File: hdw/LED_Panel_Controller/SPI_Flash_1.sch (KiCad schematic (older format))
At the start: 14 parts

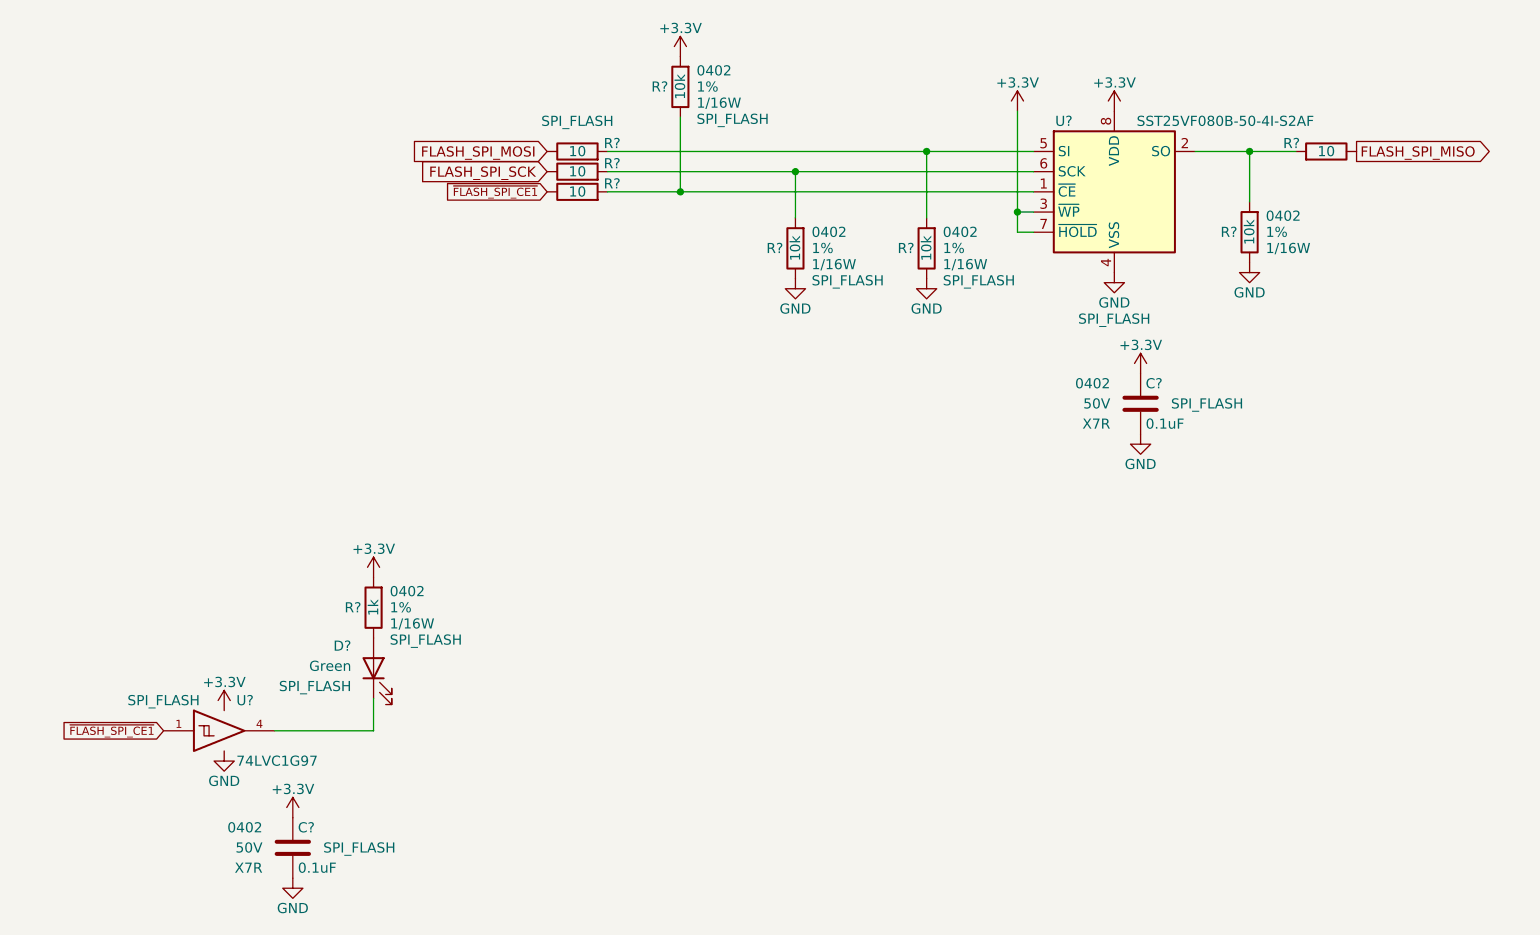
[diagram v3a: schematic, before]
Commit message: assigned I2C addresses
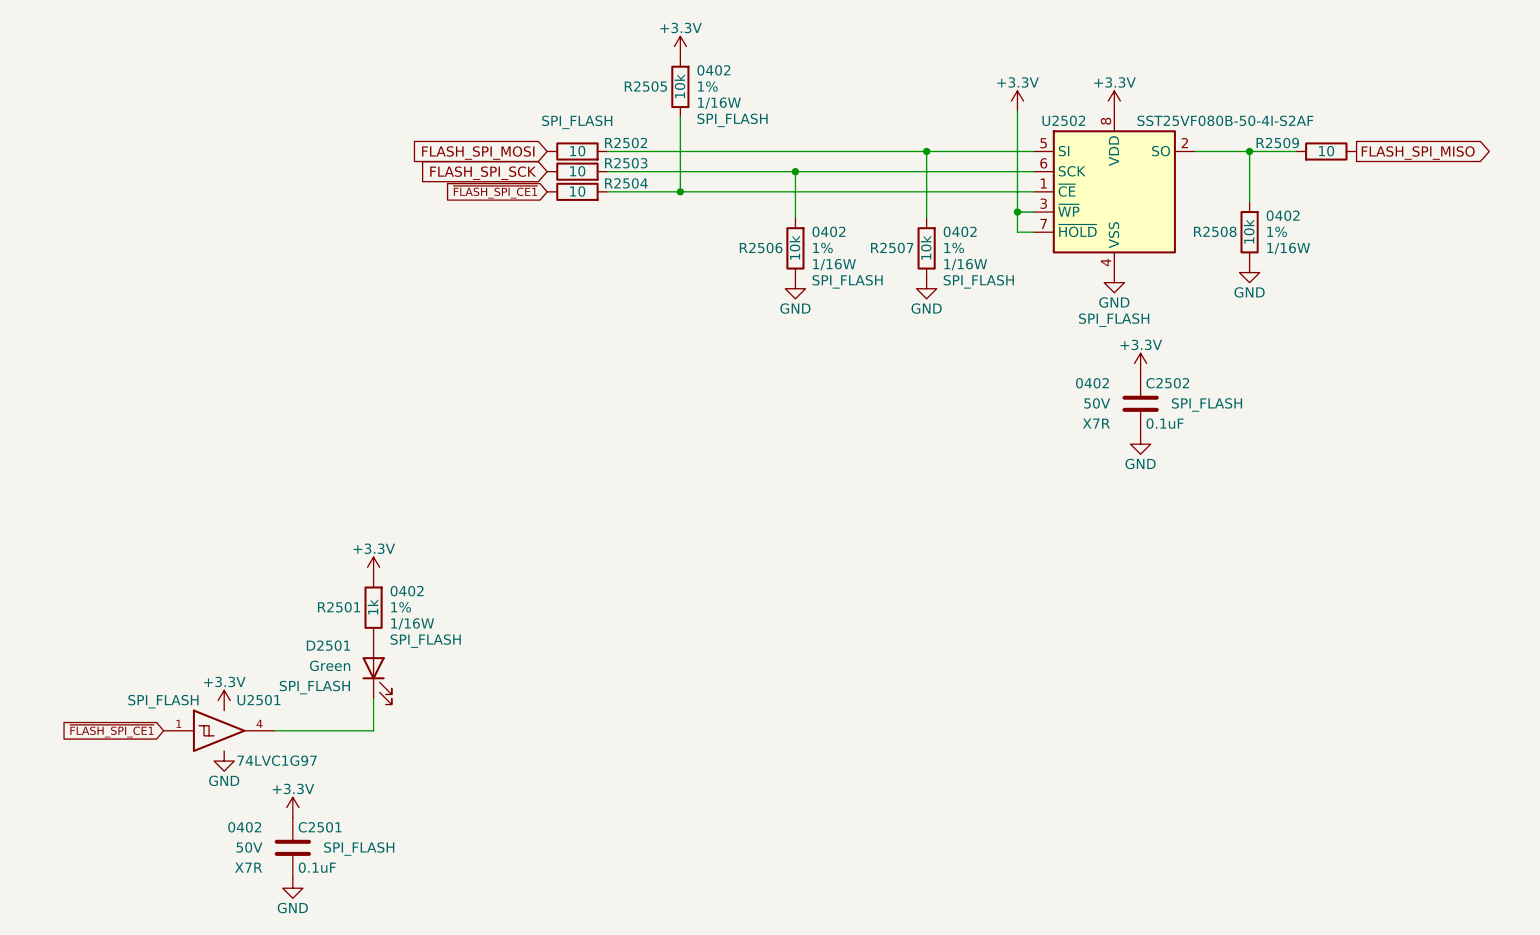
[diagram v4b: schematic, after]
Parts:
- removed C? (x2): 0.1uF, Capacitors_SMD:C_0402, symbol Custom_Library:C_Custom
- removed D?: Green, LEDs:LED_0402, symbol Device:LED
- removed R? (x4): 10, Resistors_SMD:R_0402, symbol Custom_Library:R_Custom
- removed R? (x3): 10k, Resistors_SMD:R_0402, symbol Custom_Library:R_Custom
- removed R?: 1k, Resistors_SMD:R_0402, symbol Custom_Library:R_Custom
- removed U?: 74LVC1G97, Package_TO_SOT_SMD:SOT-363_SC-70-6, symbol Custom_Library:74LVC1G97_Power_BUF
- added C2501, C2502: 0.1uF, Capacitors_SMD:C_0402, symbol Custom_Library:C_Custom
- added D2501: Green, LEDs:LED_0402, symbol Device:LED
- added R2501: 1k, Resistors_SMD:R_0402, symbol Custom_Library:R_Custom
- added R2502, R2503, R2504, R2509: 10, Resistors_SMD:R_0402, symbol Custom_Library:R_Custom
- added R2505, R2506, R2507: 10k, Resistors_SMD:R_0402, symbol Custom_Library:R_Custom
- added U2501: 74LVC1G97, Package_TO_SOT_SMD:SOT-363_SC-70-6, symbol Custom_Library:74LVC1G97_Power_BUF
- gave numbers to parts that had none: 2
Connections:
- net +3V3: now also C2501.1, C2502.1, R2501.1, R2505.1, U2501.5 (VCC)
- net FLASH_SPI_MISO: now also R2509.2
- net FLASH_SPI_MOSI: now also R2502.2
- net FLASH_SPI_SCK: now also R2503.2
- net GND: now also C2501.2, C2502.2, R2506.2, R2507.2, U2501.2 (GND), U2501.3 (GND), U2501.6 (GND)
- net ~FLASH_SPI_CE1: now also R2504.2, U2501.1
- net at R2508.1, U2502.2 (SO): now also R2509.1
- net at U2502.5 (SI): now also R2502.1, R2507.1
- net at U2502.1 (~CE): now also R2504.1, R2505.2
- net at U2502.6 (SCK): now also R2503.1, R2506.1
- new net: D2501.1 (K), U2501.4
- new net: D2501.2 (A), R2501.2
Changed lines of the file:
@@
 $EndDescr
 $Comp
-L power:GND #PWR?
+L power:GND #PWR02511
 U 1 1 5BB4E0E3
 P 6080 4050
-F 0 "#PWR?" H 6080 3800 50  0001 C CNN
+F 0 "#PWR02511" H 6080 3800 50  0001 C CNN
 F 1 "GND" H 6080 3900 50  0000 C CNN
 F 2 "" H 6080 4050 50  0001 C CNN
@@
 $EndComp
 $Comp
-L Custom_Library:R_Custom R?
+L Custom_Library:R_Custom R2508
 U 1 1 5BB4EDD1
 P 6750 3850
-F 0 "R?" H 6690 3850 50  0000 R CNN
+F 0 "R2508" H 6690 3850 50  0000 R CNN
 F 1 "10k" V 6750 3850 50  0000 C CNN
 F 2 "Resistors_SMD:R_0402" H 6750 3850 50  0001 C CNN
@@
 $EndComp
 $Comp
-L power:GND #PWR?
+L power:GND #PWR02508
 U 1 1 5BB4EE63
 P 5150 4080
-F 0 "#PWR?" H 5150 3830 50  0001 C CNN
+F 0 "#PWR02508" H 5150 3830 50  0001 C CNN
 F 1 "GND" H 5150 3930 50  0000 C CNN
 F 2 "" H 5150 4080 50  0001 C CNN
@@
 $EndComp
 $Comp
-L power:GND #PWR?
-U 1 1 5BB4EE7C
+L power:GND #PWR02514
+U 1 1 60786274
 P 6750 4000
-F 0 "#PWR?" H 6750 3750 50  0001 C CNN
+F 0 "#PWR02514" H 6750 3750 50  0001 C CNN
 F 1 "GND" H 6750 3850 50  0000 C CNN
 F 2 "" H 6750 4000 50  0001 C CNN
@@
 $EndComp
 $Comp
-L Custom_Library:R_Custom R?
-U 1 1 5BB4F53B
+L Custom_Library:R_Custom R2502
+U 1 1 6078627F
 P 3420 3450
-F 0 "R?" V 3380 3580 50  0000 L CNN
+F 0 "R2502" V 3380 3580 50  0000 L CNN
 F 1 "10" V 3420 3450 50  0000 C CNN
 F 2 "Resistors_SMD:R_0402" H 3420 3450 50  0001 C CNN
@@
 	3570 3650 3930 3650
 $Comp
-L power:+3.3V #PWR?
-U 1 1 5BDF3D33
+L power:+3.3V #PWR02506
+U 1 1 60786286
 P 3930 2980
-F 0 "#PWR?" H 3930 2830 50  0001 C CNN
+F 0 "#PWR02506" H 3930 2830 50  0001 C CNN
 F 1 "+3.3V" H 3930 3120 50  0000 C CNN
 F 2 "" H 3930 2980 50  0001 C CNN
@@
 $EndComp
 $Comp
-L power:+3.3V #PWR?
-U 1 1 5BDF3DF4
+L power:+3.3V #PWR02510
+U 1 1 6078628D
 P 6080 3250
-F 0 "#PWR?" H 6080 3100 50  0001 C CNN
+F 0 "#PWR02510" H 6080 3100 50  0001 C CNN
 F 1 "+3.3V" H 6080 3390 50  0000 C CNN
 F 2 "" H 6080 3250 50  0001 C CNN
@@
 $Comp
 L Custom_Library:C_Custom C?
-U 1 1 5C15F697
+U 1 1 60786292
 P 2010 6900
-AR Path="/5BAAE16C/5C15F697" Ref="C?"  Part="1"
-AR Path="/5BB181D8/5C15F697" Ref="C?"  Part="1"
-AR Path="/5BB2595E/5C15F697" Ref="C?"  Part="1"
-AR Path="/5F583577/5C15F697" Ref="C?"  Part="1"
-AR Path="/5F58358C/5C15F697" Ref="C?"  Part="1"
-F 0 "C?" H 2035 7000 50  0000 L CNN
+AR Path="/5BAAE16C/60786292" Ref="C?"  Part="1"
+AR Path="/5BB181D8/60786292" Ref="C?"  Part="1"
+AR Path="/5BB2595E/60786292" Ref="C?"  Part="1"
+AR Path="/5F583577/60786292" Ref="C?"  Part="1"
+AR Path="/5F58358C/60786292" Ref="C2501"  Part="1"
+F 0 "C2501" H 2035 7000 50  0000 L CNN
 F 1 "0.1uF" H 2035 6800 50  0000 L CNN
 F 2 "Capacitors_SMD:C_0402" H 2048 6750 50  0001 C CNN
@@
 $EndComp
 $Comp
-L power:+3.3V #PWR?
-U 1 1 5C161B83
+L power:+3.3V #PWR02501
+U 1 1 60786296
 P 1670 6220
-F 0 "#PWR?" H 1670 6070 50  0001 C CNN
+F 0 "#PWR02501" H 1670 6070 50  0001 C CNN
 F 1 "+3.3V" H 1670 6360 50  0000 C CNN
 F 2 "" H 1670 6220 50  0001 C CNN
@@
 $EndComp
 $Comp
-L power:+3.3V #PWR?
-U 1 1 5C161BE9
+L power:+3.3V #PWR02503
+U 1 1 607862A2
 P 2010 6750
-F 0 "#PWR?" H 2010 6600 50  0001 C CNN
+F 0 "#PWR02503" H 2010 6600 50  0001 C CNN
 F 1 "+3.3V" H 2010 6890 50  0000 C CNN
 F 2 "" H 2010 6750 50  0001 C CNN
@@
 $EndComp
 $Comp
-L power:GND #PWR?
-U 1 1 5C161C44
+L power:GND #PWR02504
+U 1 1 607862A6
 P 2010 7050
-F 0 "#PWR?" H 2010 6800 50  0001 C CNN
+F 0 "#PWR02504" H 2010 6800 50  0001 C CNN
 F 1 "GND" H 2010 6900 50  0000 C CNN
 F 2 "" H 2010 7050 50  0001 C CNN
@@
 $EndComp
 $Comp
-L power:GND #PWR?
+L power:GND #PWR02502
 U 1 1 5C161C9F
 P 1670 6420
-F 0 "#PWR?" H 1670 6170 50  0001 C CNN
+F 0 "#PWR02502" H 1670 6170 50  0001 C CNN
 F 1 "GND" H 1670 6270 50  0000 C CNN
 F 2 "" H 1670 6420 50  0001 C CNN
@@
 $Comp
 L power:+3.3V #PWR?
-U 1 1 5C166A81
+U 1 1 607862B4
 P 2410 5560
-AR Path="/5BB844FD/5C166A81" Ref="#PWR?"  Part="1"
-AR Path="/5BF346B3/5C166A81" Ref="#PWR?"  Part="1"
-AR Path="/5BB2595E/5C166A81" Ref="#PWR?"  Part="1"
-AR Path="/5F583577/5C166A81" Ref="#PWR?"  Part="1"
-AR Path="/5F58358C/5C166A81" Ref="#PWR?"  Part="1"
-F 0 "#PWR?" H 2410 5410 50  0001 C CNN
+AR Path="/5BB844FD/607862B4" Ref="#PWR?"  Part="1"
+AR Path="/5BF346B3/607862B4" Ref="#PWR?"  Part="1"
+AR Path="/5BB2595E/607862B4" Ref="#PWR?"  Part="1"
+AR Path="/5F583577/607862B4" Ref="#PWR?"  Part="1"
+AR Path="/5F58358C/607862B4" Ref="#PWR02505"  Part="1"
+F 0 "#PWR02505" H 2410 5410 50  0001 C CNN
 F 1 "+3.3V" H 2410 5700 50  0000 C CNN
 F 2 "" H 2410 5560 50  0001 C CNN
@@
 $Comp
 L Device:LED D?
-U 1 1 5C166A95
+U 1 1 607862B9
 P 2410 6010
-AR Path="/5BB844FD/5C166A95" Ref="D?"  Part="1"
-AR Path="/5BF346B3/5C166A95" Ref="D?"  Part="1"
-AR Path="/5BB2595E/5C166A95" Ref="D?"  Part="1"
-AR Path="/5F583577/5C166A95" Ref="D?"  Part="1"
-AR Path="/5F58358C/5C166A95" Ref="D?"  Part="1"
-F 0 "D?" V 2520 6120 50  0000 L CNN
+AR Path="/5BB844FD/607862B9" Ref="D?"  Part="1"
+AR Path="/5BF346B3/607862B9" Ref="D?"  Part="1"
+AR Path="/5BB2595E/607862B9" Ref="D?"  Part="1"
+AR Path="/5F583577/607862B9" Ref="D?"  Part="1"
+AR Path="/5F58358C/607862B9" Ref="D2501"  Part="1"
+F 0 "D2501" V 2520 6120 50  0000 L CNN
 F 1 "Green" V 2420 6120 50  0000 L CNN
 F 2 "LEDs:LED_0402" H 2410 6010 50  0001 C CNN
@@
 $EndComp
 $Comp
-L Memory_Flash:SST25VF080B-50-4x-S2Ax U?
+L Memory_Flash:SST25VF080B-50-4x-S2Ax U2502
 U 1 1 5F6879D5
 P 6080 3650
-F 0 "U?" H 5830 4000 50  0000 C CNN
+F 0 "U2502" H 5830 4000 50  0000 C CNN
 F 1 "SST25VF080B-50-4I-S2AF" H 6630 4000 50  0000 C CNN
 F 2 "Package_SO:SOIC-8_5.275x5.275mm_P1.27mm" H 6080 2950 50  0001 C CNN
@@
 $EndComp
 $Comp
-L power:+3.3V #PWR?
-U 1 1 5F689292
+L power:+3.3V #PWR02512
+U 1 1 60786300
 P 6210 4550
-F 0 "#PWR?" H 6210 4400 50  0001 C CNN
+F 0 "#PWR02512" H 6210 4400 50  0001 C CNN
 F 1 "+3.3V" H 6210 4690 50  0000 C CNN
 F 2 "" H 6210 4550 50  0001 C CNN
@@
 $EndComp
 $Comp
-L power:GND #PWR?
-U 1 1 5F689298
+L power:GND #PWR02513
+U 1 1 60786304
 P 6210 4850
-F 0 "#PWR?" H 6210 4600 50  0001 C CNN
+F 0 "#PWR02513" H 6210 4600 50  0001 C CNN
 F 1 "GND" H 6210 4700 50  0000 C CNN
 F 2 "" H 6210 4850 50  0001 C CNN
@@
 $EndComp
 $Comp
-L power:+3.3V #PWR?
-U 1 1 5F69329F
+L power:+3.3V #PWR02509
+U 1 1 6078630D
 P 5600 3250
-F 0 "#PWR?" H 5600 3100 50  0001 C CNN
+F 0 "#PWR02509" H 5600 3100 50  0001 C CNN
 F 1 "+3.3V" H 5600 3390 50  0000 C CNN
 F 2 "" H 5600 3250 50  0001 C CNN
@@
 	3570 3550 4500 3550
 $Comp
-L Custom_Library:R_Custom R?
-U 1 1 5F697048
+L Custom_Library:R_Custom R2506
+U 1 1 60786317
 P 4500 3930
-F 0 "R?" H 4440 3930 50  0000 R CNN
+F 0 "R2506" H 4440 3930 50  0000 R CNN
 F 1 "10k" V 4500 3930 50  0000 C CNN
 F 2 "Resistors_SMD:R_0402" H 4500 3930 50  0001 C CNN
@@
 $EndComp
 $Comp
-L power:GND #PWR?
-U 1 1 5F697052
+L power:GND #PWR02507
+U 1 1 6078631C
 P 4500 4080
-F 0 "#PWR?" H 4500 3830 50  0001 C CNN
+F 0 "#PWR02507" H 4500 3830 50  0001 C CNN
 F 1 "GND" H 4500 3930 50  0000 C CNN
 F 2 "" H 4500 4080 50  0001 C CNN
@@
 	4500 3550 5680 3550
 $Comp
-L Custom_Library:R_Custom R?
-U 1 1 5F7379BB
+L Custom_Library:R_Custom R2503
+U 1 1 60786326
 P 3420 3550
-F 0 "R?" V 3380 3680 50  0000 L CNN
+F 0 "R2503" V 3380 3680 50  0000 L CNN
 F 1 "10" V 3420 3550 50  0000 C CNN
 F 2 "Resistors_SMD:R_0402" H 3420 3550 50  0001 C CNN
@@
 $EndComp
 $Comp
-L Custom_Library:R_Custom R?
-U 1 1 5F737B74
+L Custom_Library:R_Custom R2504
+U 1 1 60786328
 P 3420 3650
-F 0 "R?" V 3380 3780 50  0000 L CNN
+F 0 "R2504" V 3380 3780 50  0000 L CNN
 F 1 "10" V 3420 3650 50  0000 C CNN
 F 2 "Resistors_SMD:R_0402" H 3420 3650 50  0001 C CNN
@@
 $EndComp
 $Comp
-L Custom_Library:R_Custom R?
-U 1 1 5F737D15
+L Custom_Library:R_Custom R2509
+U 1 1 60786330
 P 7130 3450
-F 0 "R?" V 7090 3580 50  0000 L CNN
+F 0 "R2509" V 7090 3580 50  0000 L CNN
 F 1 "10" V 7130 3450 50  0000 C CNN
 F 2 "Resistors_SMD:R_0402" H 7130 3450 50  0001 C CNN
@@
 $EndComp
 $Comp
-L Custom_Library:74LVC1G97_Power_BUF U?
-U 1 1 5FE9D8D5
+L Custom_Library:74LVC1G97_Power_BUF U2501
+U 1 1 60786346
 P 1670 6320
-F 0 "U?" H 1730 6470 50  0000 L CNN
+F 0 "U2501" H 1730 6470 50  0000 L CNN
 F 1 "74LVC1G97" H 1730 6170 50  0000 L CNN
 F 2 "Package_TO_SOT_SMD:SOT-363_SC-70-6" H 1720 6320 50  0001 C CNN
@@
 $EndComp
 $Comp
-L Custom_Library:R_Custom R?
-U 1 1 6026393A
+L Custom_Library:R_Custom R2507
+U 1 1 6078635A
 P 5150 3930
-F 0 "R?" H 5090 3930 50  0000 R CNN
+F 0 "R2507" H 5090 3930 50  0000 R CNN
 F 1 "10k" V 5150 3930 50  0000 C CNN
 F 2 "Resistors_SMD:R_0402" H 5150 3930 50  0001 C CNN
@@
 $EndComp
 $Comp
-L Custom_Library:R_Custom R?
-U 1 1 60263FB7
+L Custom_Library:R_Custom R2505
+U 1 1 6078635D
 P 3930 3130
-F 0 "R?" H 3870 3130 50  0000 R CNN
+F 0 "R2505" H 3870 3130 50  0000 R CNN
 F 1 "10k" V 3930 3130 50  0000 C CNN
 F 2 "Resistors_SMD:R_0402" H 3930 3130 50  0001 C CNN
@@
 $EndComp
 $Comp
-L Custom_Library:R_Custom R?
-U 1 1 60266213
+L Custom_Library:R_Custom R2501
+U 1 1 60786363
 P 2410 5710
-F 0 "R?" H 2350 5710 50  0000 R CNN
+F 0 "R2501" H 2350 5710 50  0000 R CNN
 F 1 "1k" V 2410 5710 50  0000 C CNN
 F 2 "Resistors_SMD:R_0402" H 2410 5710 50  0001 C CNN
@@
 $Comp
 L Custom_Library:C_Custom C?
-U 1 1 60269564
+U 1 1 6078636E
 P 6210 4700
-AR Path="/5BAAE16C/60269564" Ref="C?"  Part="1"
-AR Path="/5BB181D8/60269564" Ref="C?"  Part="1"
-AR Path="/5BB2595E/60269564" Ref="C?"  Part="1"
-AR Path="/5F583577/60269564" Ref="C?"  Part="1"
-AR Path="/5F58358C/60269564" Ref="C?"  Part="1"
-F 0 "C?" H 6235 4800 50  0000 L CNN
+AR Path="/5BAAE16C/6078636E" Ref="C?"  Part="1"
+AR Path="/5BB181D8/6078636E" Ref="C?"  Part="1"
+AR Path="/5BB2595E/6078636E" Ref="C?"  Part="1"
+AR Path="/5F583577/6078636E" Ref="C?"  Part="1"
+AR Path="/5F58358C/6078636E" Ref="C2502"  Part="1"
+F 0 "C2502" H 6235 4800 50  0000 L CNN
 F 1 "0.1uF" H 6235 4600 50  0000 L CNN
 F 2 "Capacitors_SMD:C_0402" H 6248 4550 50  0001 C CNN
